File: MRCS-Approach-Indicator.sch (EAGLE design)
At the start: 17 parts, among them J1 5 VDC, J2 Output, J3 Station 0, J4 Station 1, J5 Stations 2 and 3, J6 relay out, K1 G6H2-100, K2 G6H2-100, K3 G6H2-100, K4 G6H2-100

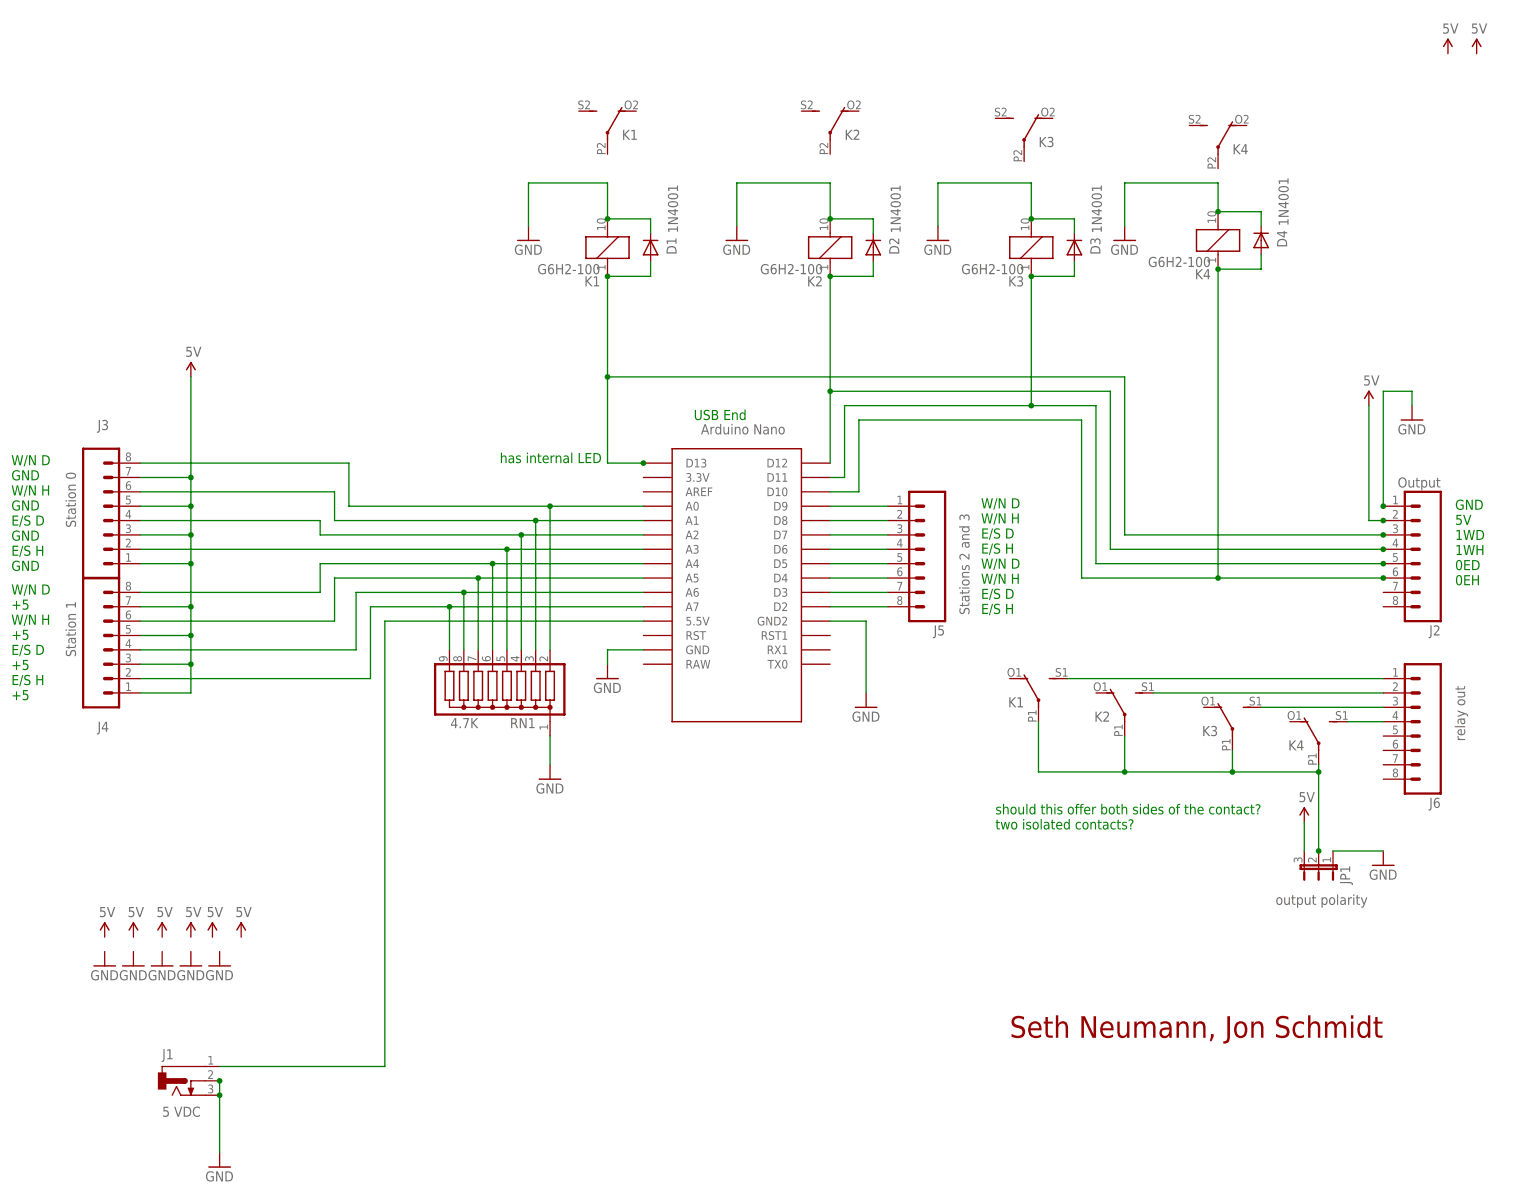
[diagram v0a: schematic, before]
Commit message: changes after design review
- changed contacts to dry pairs with grounding jumper
- added LEDs for relay status
- re-arranged raw logic outputs and added another +5/GND pair
- fixed label issues
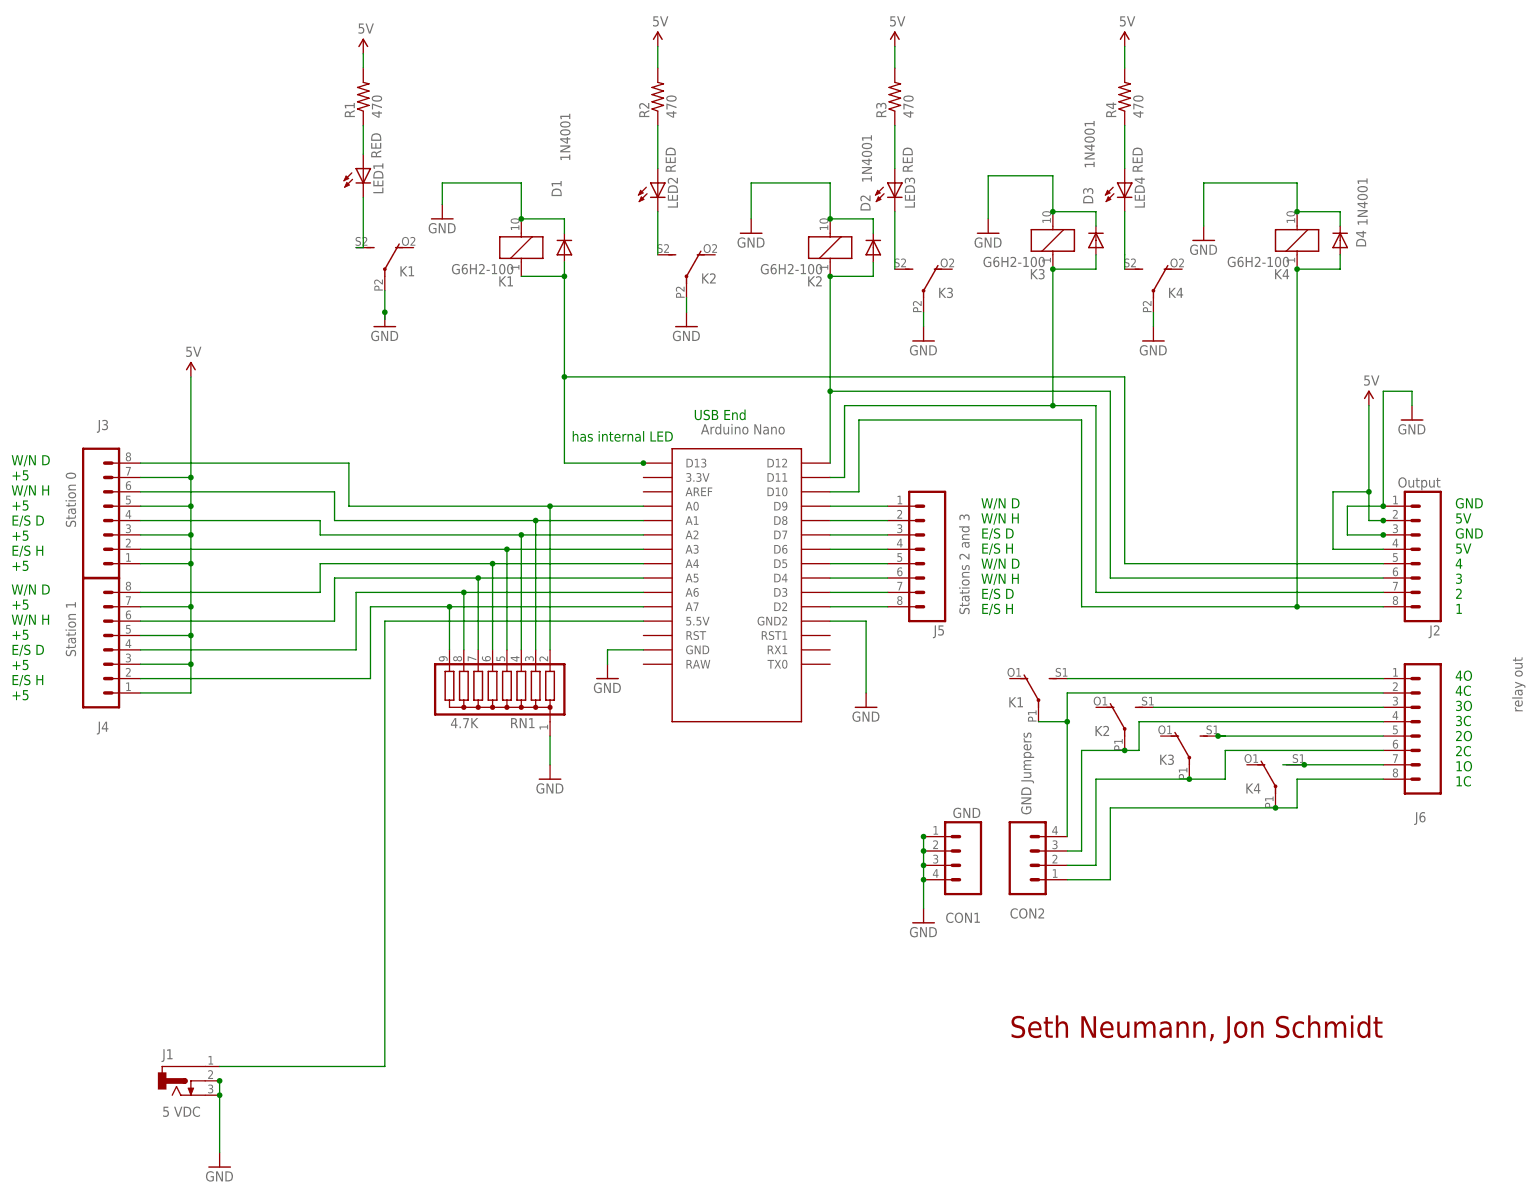
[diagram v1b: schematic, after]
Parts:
- removed JP1: output polarity, SPCoast:JUMPER-3PTH-LOCK
- added CON1: GND, SPCoast:CONNECTOR-M04LOCK
- added CON2: GND Jumpers, SPCoast:CONNECTOR-M04LOCK
- added LED1, LED2, LED3, LED4: RED, SPCoast:LEDLED3MM
- added R1, R2, R3, R4: 470, SPCoast:RPTH04
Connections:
- removed net D11: D3.A, J2.5, K31.1, NANO.D11
- new net N$1: J6.3, K22.S
- new net N$24: J6.7, K42.S
- new net N$25: CON2.1, J6.8, K42.P
- new net N$26: K13.S, LED1.C
- new net N$27: LED1.A, R1.1
- new net N$28: LED2.A, R2.1
- new net N$29: K23.S, LED2.C
- new net N$30: LED3.A, R3.1
- new net N$31: K33.S, LED3.C
- new net N$32: LED4.A, R4.1
- new net N$33: K43.S, LED4.C
- new net N$34: D3.A, J2.7, K31.1, NANO.D11
- net 5V: now also J2.4, R1.2, R2.2, R3.2, R4.2; no longer JP1.3
- net D12: now also J2.6; no longer J2.4
- net D7: now also J2.5; no longer J2.3
- net GND: now also CON1.1, CON1.2, CON1.3, CON1.4, J2.3, K13.P, K23.P, K33.P, K43.P; no longer JP1.1
- net N$2: now also J2.8; no longer J2.6
- net N$21: now also J6.5; no longer J6.3
- net N$22: now also CON2.4, J6.2, K12.P; no longer J6.4, K42.S
- net N$23: now also CON2.2, J6.6; no longer JP1.2, K12.P, K22.P, K42.P
- net N$8: now also CON2.3, J6.4, K22.P; no longer J6.2, K22.S
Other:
- note added: "4O 4C 3O 3C 2O 2C 1O 1C"
- note added: "GND 5V GND 5V 4 3 2 1"
- note removed: "GND 5V 1WD 1WH 0ED 0EH"
- note removed: "W/N D GND W/N H GND E/S D GND E/S H GND"
- note removed: "should this offer both sides of the contact? two isolated contacts?"
- moved on the sheet: D1, D3, D4, K1, K2, K3, K4

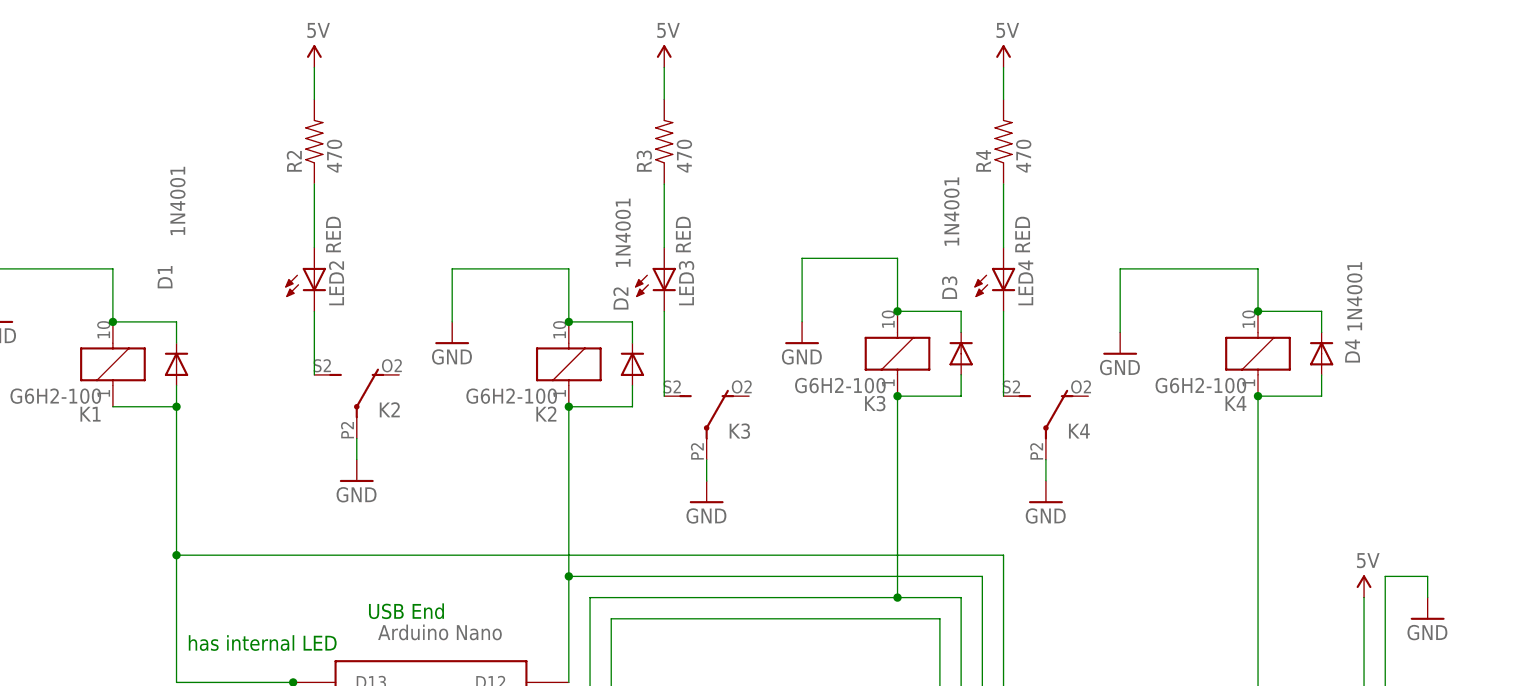
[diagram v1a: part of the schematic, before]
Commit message: Order as submitter to JLCPCB
Changes after design review with Jon Schmidt, various label clean up items.  Thanks to John Plocher for suggestions on managing back side labels and logos!
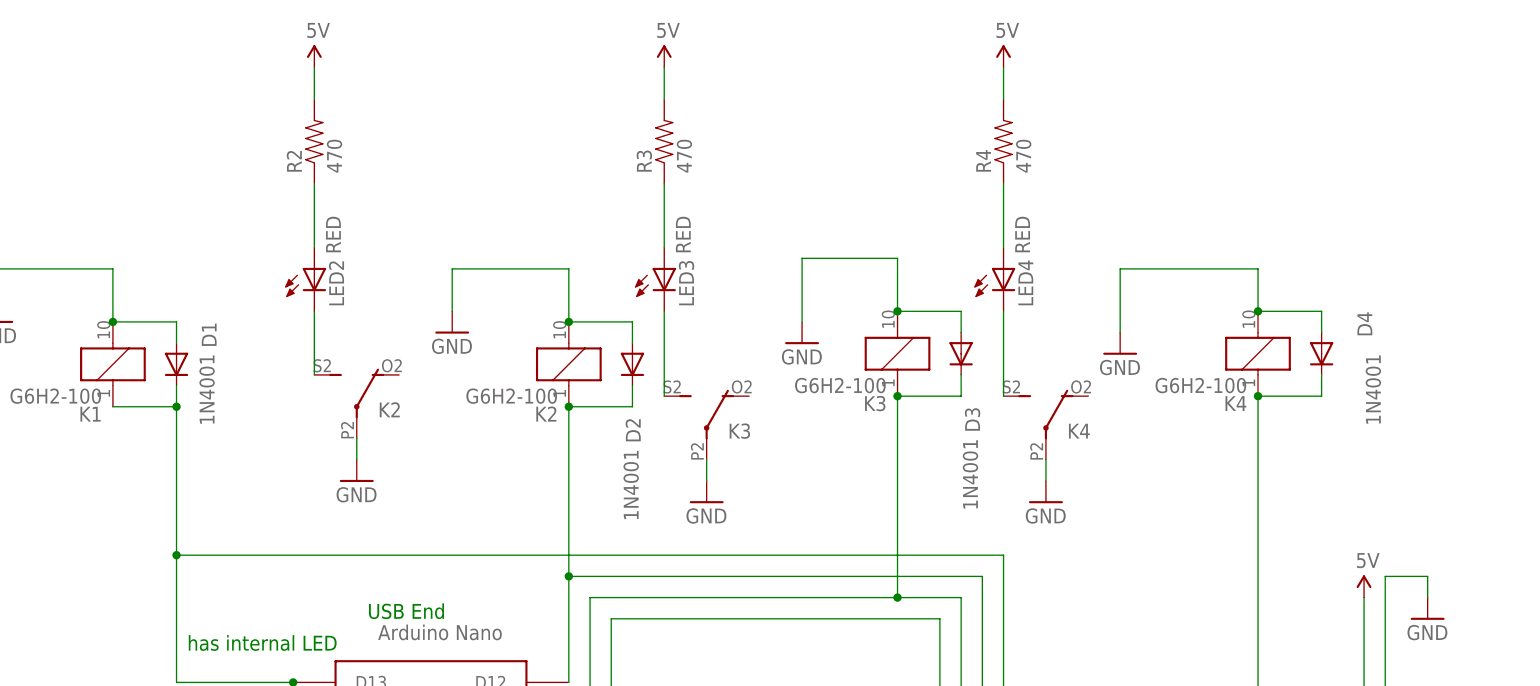
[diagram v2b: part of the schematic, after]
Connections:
- net D12: now also D2.C; no longer D2.A
- net D7: now also D1.C; no longer D1.A
- net GND: now also D1.A, D2.A, D3.A, D4.A; no longer D1.C, D2.C, D3.C, D4.C
- net N$2: now also D4.C; no longer D4.A
- net N$34: now also D3.C; no longer D3.A
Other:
- moved on the sheet: D1, D2, D3, D4
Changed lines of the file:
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@@
 <instance part="GND1" gate="1" x="86.36" y="81.28"/>
 <instance part="SUPPLY9" gate="G$1" x="220.98" y="129.54"/>
-<instance part="GND4" gate="1" x="111.76" y="160.02"/>
+<instance part="GND4" gate="1" x="111.76" y="161.29"/>
 <instance part="GND6" gate="1" x="17.78" y="-5.08"/>
 <instance part="GND7" gate="1" x="228.6" y="127"/>
@@
 <attribute name="NAME" x="231.14" y="57.658" size="1.778" layer="95" rot="R180"/>
 </instance>
-<instance part="D1" gate="D1" x="78.74" y="157.48" smashed="yes" rot="R90">
-<attribute name="NAME" x="78.2574" y="166.37" size="1.778" layer="95" rot="R90"/>
-<attribute name="VALUE" x="79.7814" y="172.72" size="1.778" layer="96" rot="R90"/>
-</instance>
-<instance part="D2" gate="D1" x="133.35" y="157.48" smashed="yes" rot="R90">
-<attribute name="NAME" x="132.8674" y="163.83" size="1.778" layer="95" rot="R90"/>
-<attribute name="VALUE" x="133.1214" y="168.91" size="1.778" layer="96" rot="R90"/>
-</instance>
-<instance part="D3" gate="D1" x="172.72" y="158.75" smashed="yes" rot="R90">
-<attribute name="NAME" x="172.2374" y="165.1" size="1.778" layer="95" rot="R90"/>
-<attribute name="VALUE" x="172.4914" y="171.45" size="1.778" layer="96" rot="R90"/>
-</instance>
-<instance part="D4" gate="D1" x="215.9" y="158.75" smashed="yes" rot="R90">
-<attribute name="NAME" x="220.4974" y="157.48" size="1.778" layer="95" rot="R90"/>
-<attribute name="VALUE" x="220.7514" y="161.29" size="1.778" layer="96" rot="R90"/>
+<instance part="D1" gate="D1" x="78.74" y="157.48" smashed="yes" rot="R270">
+<attribute name="NAME" x="81.7626" y="162.56" size="1.778" layer="95" rot="R270"/>
+<attribute name="VALUE" x="81.5086" y="158.75" size="1.778" layer="96" rot="R270"/>
+</instance>
+<instance part="D2" gate="D1" x="133.35" y="157.48" smashed="yes" rot="R270">
+<attribute name="NAME" x="132.5626" y="151.13" size="1.778" layer="95" rot="R270"/>
+<attribute name="VALUE" x="132.3086" y="147.32" size="1.778" layer="96" rot="R270"/>
+</instance>
+<instance part="D3" gate="D1" x="172.72" y="158.75" smashed="yes" rot="R270">
+<attribute name="NAME" x="173.2026" y="152.4" size="1.778" layer="95" rot="R270"/>
+<attribute name="VALUE" x="172.9486" y="148.59" size="1.778" layer="96" rot="R270"/>
+</instance>
+<instance part="D4" gate="D1" x="215.9" y="158.75" smashed="yes" rot="R270">
+<attribute name="NAME" x="220.1926" y="163.83" size="1.778" layer="95" rot="R270"/>
+<attribute name="VALUE" x="221.2086" y="158.75" size="1.778" layer="96" rot="R270"/>
 </instance>
 <instance part="RN1" gate="G$1" x="66.04" y="81.28" rot="R180"/>
@@
 <pinref part="K1" gate="1" pin="2"/>
 <wire x1="71.12" y1="168.91" x2="71.12" y2="162.56" width="0.3048" layer="91"/>
-<pinref part="D1" gate="D1" pin="C"/>
-<wire x1="78.74" y1="160.02" x2="78.74" y2="162.56" width="0.3048" layer="91"/>
 <wire x1="78.74" y1="162.56" x2="71.12" y2="162.56" width="0.3048" layer="91"/>
 <junction x="71.12" y="162.56"/>
+<pinref part="D1" gate="D1" pin="A"/>
+<wire x1="78.74" y1="162.56" x2="78.74" y2="160.02" width="0.3048" layer="91"/>
 </segment>
 <segment>
 <pinref part="GND4" gate="1" pin="GND"/>
-<wire x1="111.76" y1="162.56" x2="111.76" y2="168.91" width="0.3048" layer="91"/>
+<wire x1="111.76" y1="163.83" x2="111.76" y2="168.91" width="0.3048" layer="91"/>
 <wire x1="111.76" y1="168.91" x2="125.73" y2="168.91" width="0.3048" layer="91"/>
 <pinref part="K2" gate="1" pin="2"/>
 <wire x1="125.73" y1="168.91" x2="125.73" y2="162.56" width="0.3048" layer="91"/>
-<pinref part="D2" gate="D1" pin="C"/>
-<wire x1="133.35" y1="160.02" x2="133.35" y2="162.56" width="0.3048" layer="91"/>
 <wire x1="133.35" y1="162.56" x2="125.73" y2="162.56" width="0.3048" layer="91"/>
 <junction x="125.73" y="162.56"/>
+<pinref part="D2" gate="D1" pin="A"/>
+<wire x1="133.35" y1="162.56" x2="133.35" y2="160.02" width="0.3048" layer="91"/>
 </segment>
 <segment>
@@
 <pinref part="GND17" gate="1" pin="GND"/>
 <wire x1="153.67" y1="170.18" x2="153.67" y2="162.56" width="0.3048" layer="91"/>
-<pinref part="D3" gate="D1" pin="C"/>
-<wire x1="172.72" y1="161.29" x2="172.72" y2="163.83" width="0.3048" layer="91"/>
-<wire x1="172.72" y1="163.83" x2="165.1" y2="163.83" width="0.3048" layer="91"/>
+<wire x1="165.1" y1="163.83" x2="172.72" y2="163.83" width="0.3048" layer="91"/>
+<pinref part="D3" gate="D1" pin="A"/>
+<wire x1="172.72" y1="163.83" x2="172.72" y2="161.29" width="0.3048" layer="91"/>
 <junction x="165.1" y="163.83"/>
 </segment>
@@
 <pinref part="K4" gate="1" pin="2"/>
 <wire x1="208.28" y1="168.91" x2="208.28" y2="163.83" width="0.3048" layer="91"/>
-<pinref part="D4" gate="D1" pin="C"/>
-<wire x1="215.9" y1="161.29" x2="215.9" y2="163.83" width="0.3048" layer="91"/>
 <wire x1="215.9" y1="163.83" x2="208.28" y2="163.83" width="0.3048" layer="91"/>
 <junction x="208.28" y="163.83"/>
+<pinref part="D4" gate="D1" pin="A"/>
+<wire x1="215.9" y1="163.83" x2="215.9" y2="161.29" width="0.3048" layer="91"/>
 </segment>
 <segment>
@@
 <junction x="165.1" y="129.54"/>
 <wire x1="165.1" y1="153.67" x2="172.72" y2="153.67" width="0.3048" layer="91"/>
-<pinref part="D3" gate="D1" pin="A"/>
-<wire x1="172.72" y1="153.67" x2="172.72" y2="156.21" width="0.3048" layer="91"/>
 <junction x="165.1" y="153.67"/>
 <wire x1="172.72" y1="96.52" x2="223.52" y2="96.52" width="0.3048" layer="91"/>
 <pinref part="J2" gate="G$1" pin="7"/>
+<pinref part="D3" gate="D1" pin="C"/>
+<wire x1="172.72" y1="156.21" x2="172.72" y2="153.67" width="0.3048" layer="91"/>
 </segment>
 </net>
@@
 <junction x="125.73" y="132.08"/>
 <wire x1="125.73" y1="152.4" x2="133.35" y2="152.4" width="0.3048" layer="91"/>
-<pinref part="D2" gate="D1" pin="A"/>
-<wire x1="133.35" y1="152.4" x2="133.35" y2="154.94" width="0.3048" layer="91"/>
 <junction x="125.73" y="152.4"/>
 <pinref part="J2" gate="G$1" pin="6"/>
 <wire x1="175.26" y1="99.06" x2="223.52" y2="99.06" width="0.3048" layer="91"/>
+<pinref part="D2" gate="D1" pin="C"/>
+<wire x1="133.35" y1="154.94" x2="133.35" y2="152.4" width="0.3048" layer="91"/>
 </segment>
 </net>
@@
 <junction x="92.71" y="119.38"/>
 <pinref part="K1" gate="1" pin="1"/>
-<pinref part="D1" gate="D1" pin="A"/>
-<wire x1="78.74" y1="154.94" x2="78.74" y2="152.4" width="0.3048" layer="91"/>
 <wire x1="78.74" y1="152.4" x2="71.12" y2="152.4" width="0.3048" layer="91"/>
 <wire x1="78.74" y1="152.4" x2="78.74" y2="134.62" width="0.3048" layer="91"/>
-<junction x="78.74" y="152.4"/>
 <junction x="78.74" y="134.62"/>
 <pinref part="J2" gate="G$1" pin="5"/>
 <wire x1="223.52" y1="101.6" x2="177.8" y2="101.6" width="0.3048" layer="91"/>
+<pinref part="D1" gate="D1" pin="C"/>
+<wire x1="78.74" y1="154.94" x2="78.74" y2="152.4" width="0.3048" layer="91"/>
+<junction x="78.74" y="152.4"/>
 </segment>
 </net>
@@
 <wire x1="208.28" y1="153.67" x2="208.28" y2="93.98" width="0.3048" layer="91"/>
 <wire x1="208.28" y1="153.67" x2="215.9" y2="153.67" width="0.3048" layer="91"/>
-<pinref part="D4" gate="D1" pin="A"/>
-<wire x1="215.9" y1="153.67" x2="215.9" y2="156.21" width="0.3048" layer="91"/>
 <junction x="208.28" y="153.67"/>
 <wire x1="208.28" y1="93.98" x2="223.52" y2="93.98" width="0.3048" layer="91"/>
 <junction x="208.28" y="93.98"/>
 <pinref part="J2" gate="G$1" pin="8"/>
-</segment>
-</net>
+<pinref part="D4" gate="D1" pin="C"/>
+<wire x1="215.9" y1="156.21" x2="215.9" y2="153.67" width="0.3048" layer="91"/>
+</segment>
+</net>

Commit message: label corrections
changes to labels to align better with code, note some board designations are different than schematic
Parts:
- renumbered K4 to K0, LED4 to LED0
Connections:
- net D7: now also K31.1; no longer K11.1
- net N$21: now also K12.S; no longer K32.S
- net N$22: now also K32.P; no longer K12.P
- net N$23: now also K12.P; no longer K32.P
- net N$27: now also LED3.A; no longer LED1.A
- net N$30: now also LED1.A; no longer LED3.A
- net N$34: now also K11.1; no longer K31.1
- net N$7: now also K32.S; no longer K12.S
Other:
- moved on the sheet: K1, K3, LED1, LED3
